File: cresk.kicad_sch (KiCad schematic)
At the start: 38 parts, among them J1 8P8C, J2 8P8C, SW1 SW_PUSH, SW10 SW_PUSH, SW11 SW_PUSH, SW12 SW_PUSH, SW13 SW_PUSH, SW14 SW_PUSH, SW15 SW_PUSH, SW16 SW_PUSH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

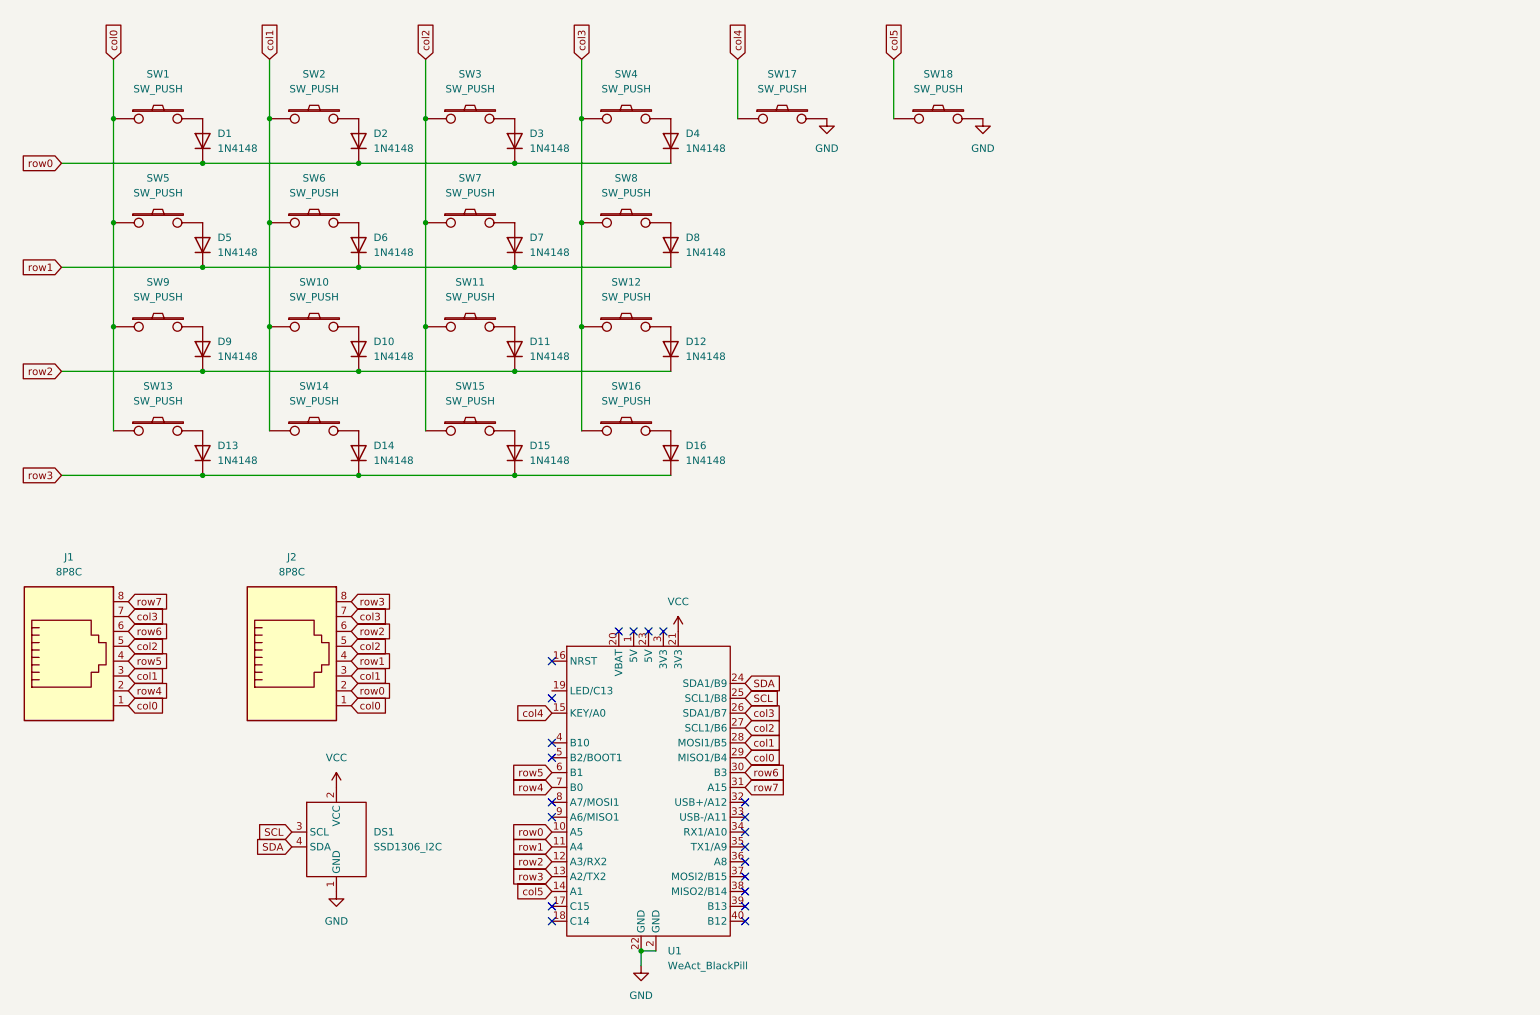
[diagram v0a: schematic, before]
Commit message: feat: replace cresk with cresk v2
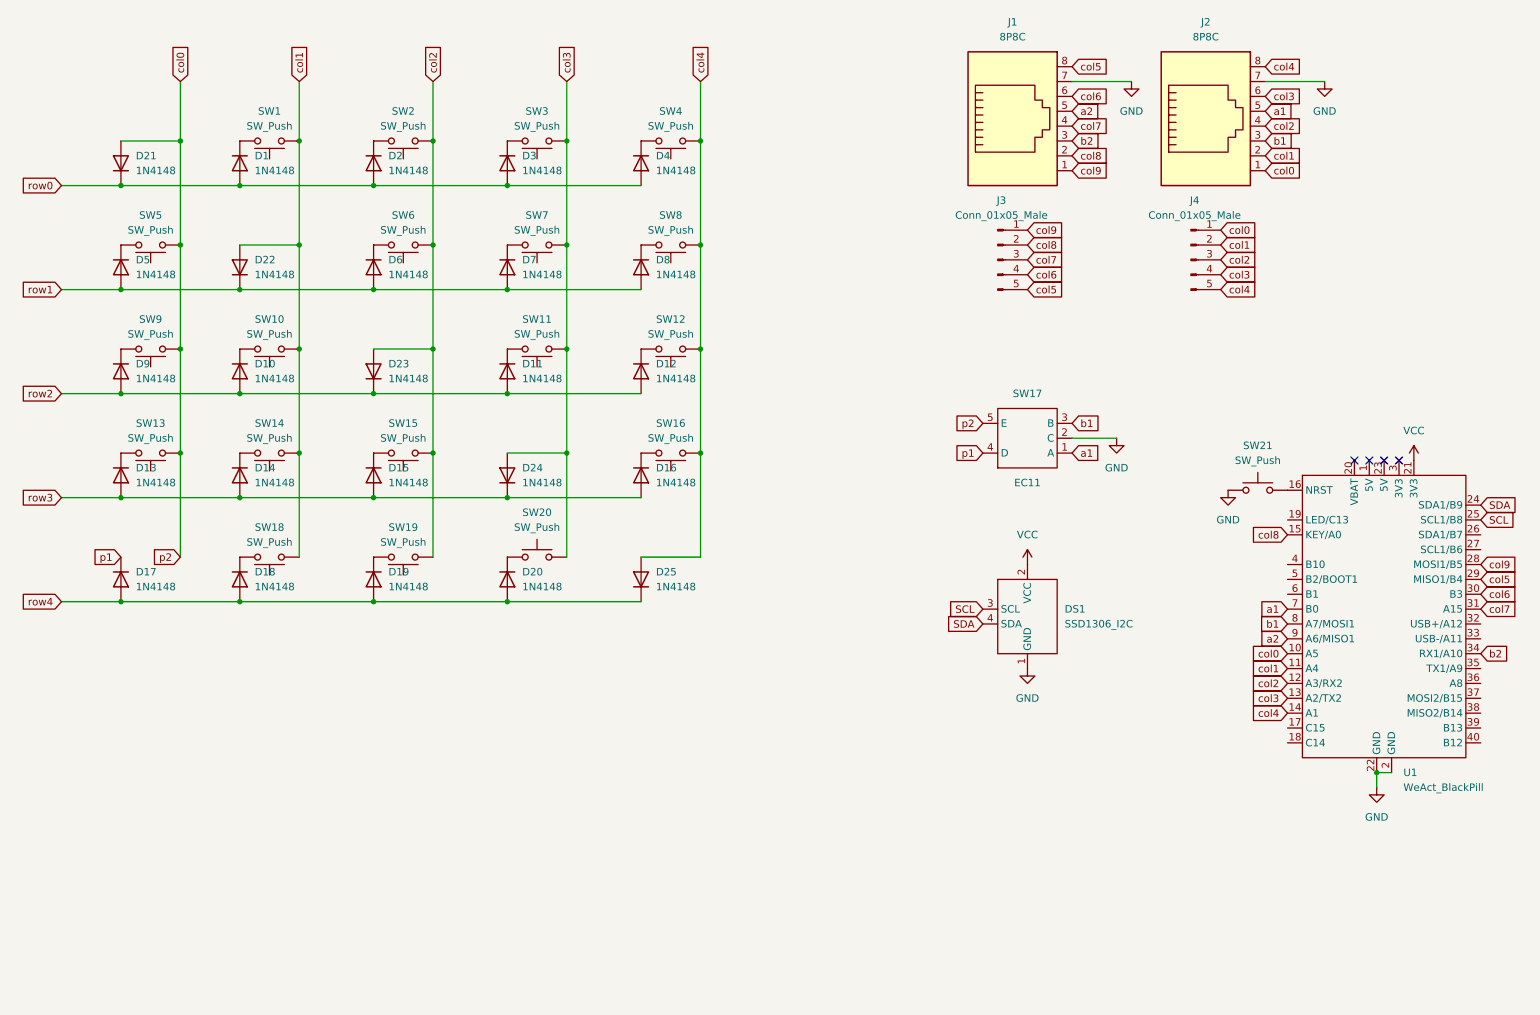
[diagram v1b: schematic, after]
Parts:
- removed SW1, SW10, SW11, SW12, SW13, SW14, SW15, SW16, SW17, SW18, SW2, SW3, SW4, SW5, SW6, SW7, SW8, SW9: SW_PUSH, symbol cresk:SW_PUSH
- added D17, D18, D19, D20, D21, D22, D23, D24, D25: 1N4148, cresk:D_DO-35, symbol Diode:1N4148
- added J3, J4: Conn_01x05_Male, cresk:J-01x05, symbol Connector:Conn_01x05_Male
- added SW1, SW10, SW11, SW12, SW13, SW14, SW15, SW16, SW18, SW19, SW2, SW20, SW3, SW4, SW5, SW6, SW7, SW8, SW9: SW_Push, cresk:SW_MX_1u_Reversible, symbol Switch:SW_Push
- added SW17: EC11, cresk:EC11, symbol cresk:EC11
- added SW21: SW_Push, Button_Switch_THT:SW_PUSH_6mm, symbol Switch:SW_Push
- D1, D10, D11, D12, D13, D14, D15, D16, D2, D3, D4, D5, D6, D7, D8, D9: footprint Diode_THT:D_DO-35_SOD27_P7.62mm_Horizontal -> cresk:D_DO-35
- J1, J2: footprint Connector_RJ:RJ45_Amphenol_54602-x08_Horizontal -> Connector_RJ:RJ45_Ninigi_GE
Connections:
- net GND: now also J1.7, J2.7, SW17.2 (C), SW21.1
- net col0: now also U1.10 (A5), D21.2 (A), J4.1 (Pin_1), SW13.1, SW17.5 (E), SW5.1, SW9.1; no longer J1.1, U1.29 (MISO1/B4)
- net col1: now also J2.2, U1.11 (A4), D22.2 (A), J4.2 (Pin_2), SW1.1, SW10.1, SW14.1, SW18.1; no longer J1.3, J2.3, U1.28 (MOSI1/B5)
- net col2: now also J2.4, U1.12 (A3/RX2), D23.2 (A), J4.3 (Pin_3), SW15.1, SW19.1, SW2.1, SW6.1; no longer J1.5, J2.5, U1.27 (SCL1/B6)
- net col3: now also J2.6, U1.13 (A2/TX2), D24.2 (A), J4.4 (Pin_4), SW11.1, SW20.2, SW3.1, SW7.1; no longer J1.7, J2.7, U1.26 (SDA1/B7)
- net col4: now also J2.8, U1.14 (A1), D25.2 (A), J4.5 (Pin_5), SW12.1, SW16.1, SW4.1, SW8.1; no longer U1.15 (KEY/A0)
- net col5: now also J1.8, U1.29 (MISO1/B4), J3.5 (Pin_5); no longer U1.14 (A1)
- net row0: now also D1.2 (A), D2.2 (A), D3.2 (A), D4.2 (A), D21.1 (K); no longer D1.1 (K), D2.1 (K), D3.1 (K), D4.1 (K), J2.2, U1.10 (A5)
- net row1: now also D5.2 (A), D6.2 (A), D7.2 (A), D8.2 (A), D22.1 (K); no longer D5.1 (K), D6.1 (K), D7.1 (K), D8.1 (K), J2.4, U1.11 (A4)
- net row2: now also D10.2 (A), D11.2 (A), D12.2 (A), D9.2 (A), D23.1 (K); no longer D10.1 (K), D11.1 (K), D12.1 (K), D9.1 (K), J2.6, U1.12 (A3/RX2)
- net row3: now also D13.2 (A), D14.2 (A), D15.2 (A), D16.2 (A), D24.1 (K); no longer D13.1 (K), D14.1 (K), D15.1 (K), D16.1 (K), J2.8, U1.13 (A2/TX2)
- net row4: now also D17.2 (A), D18.2 (A), D19.2 (A), D20.2 (A), D25.1 (K); no longer J1.2, U1.7 (B0)
- net at U1.16 (NRST): now also SW21.2
- net b2: now reaches U1.34 (RX1/A10)
- net b2: now also J1.3
- net b1: now reaches U1.8 (A7/MOSI1)
- net b1: now also J2.3, SW17.3 (B)
- net a2: now reaches U1.9 (A6/MISO1)
- net a2: now also J1.5
- net row5: no longer names the net of U1.6 (B1)
- net row5: no longer J1.4
- net row6 renamed col6
- net col6: now also J3.4 (Pin_4)
- net row7 renamed col7
- net col7: now also J1.4, J3.3 (Pin_3); no longer J1.8
- new net: D15.1 (K), SW15.2
- new net: D3.1 (K), SW3.2
- new net: D20.1 (K), SW20.1
- new net: D9.1 (K), SW9.2
- new net: D8.1 (K), SW8.2
- new net: D13.1 (K), SW13.2
- new net: D5.1 (K), SW5.2
- new net: D16.1 (K), SW16.2
- new net: D4.1 (K), SW4.2
- new net: D12.1 (K), SW12.2
- new net: D14.1 (K), SW14.2
- new net: D11.1 (K), SW11.2
- new net: D1.1 (K), SW1.2
- new net: D6.1 (K), SW6.2
- new net: D7.1 (K), SW7.2
- new net: D18.1 (K), SW18.2
- new net: D2.1 (K), SW2.2
- new net: D10.1 (K), SW10.2
- new net: D19.1 (K), SW19.2
- new net a1: J2.5, SW17.1 (A), U1.7 (B0)
- new net col8: J1.2, J3.2 (Pin_2), U1.15 (KEY/A0)
- new net col9: J1.1, J3.1 (Pin_1), U1.28 (MOSI1/B5)
- new net p1: D17.1 (K), SW17.4 (D)
- no-connect marks 21 -> 4
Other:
- moved on the sheet: DS1, J1, J2, U1
